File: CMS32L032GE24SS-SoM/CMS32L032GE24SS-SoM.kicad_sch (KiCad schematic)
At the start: 7 parts, among them J105 Connection to DAPLink Board

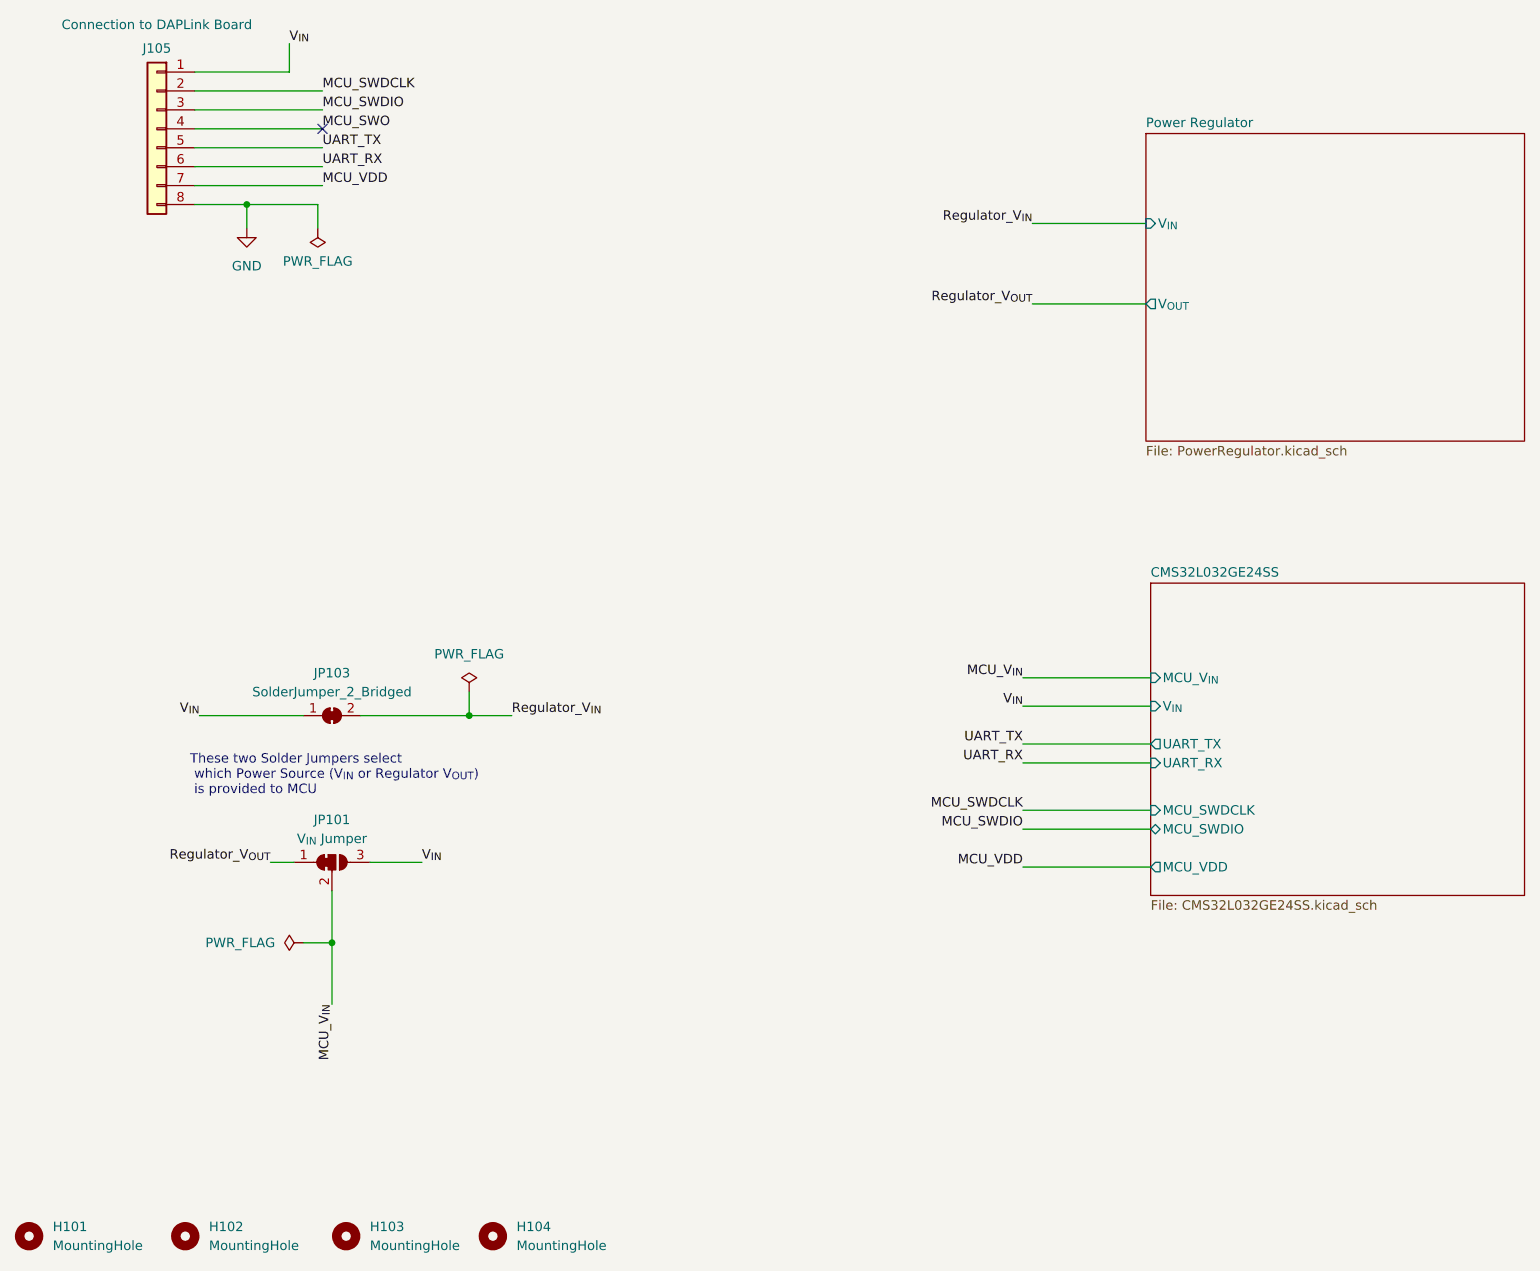
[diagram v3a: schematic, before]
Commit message: changed Power Source jumpers
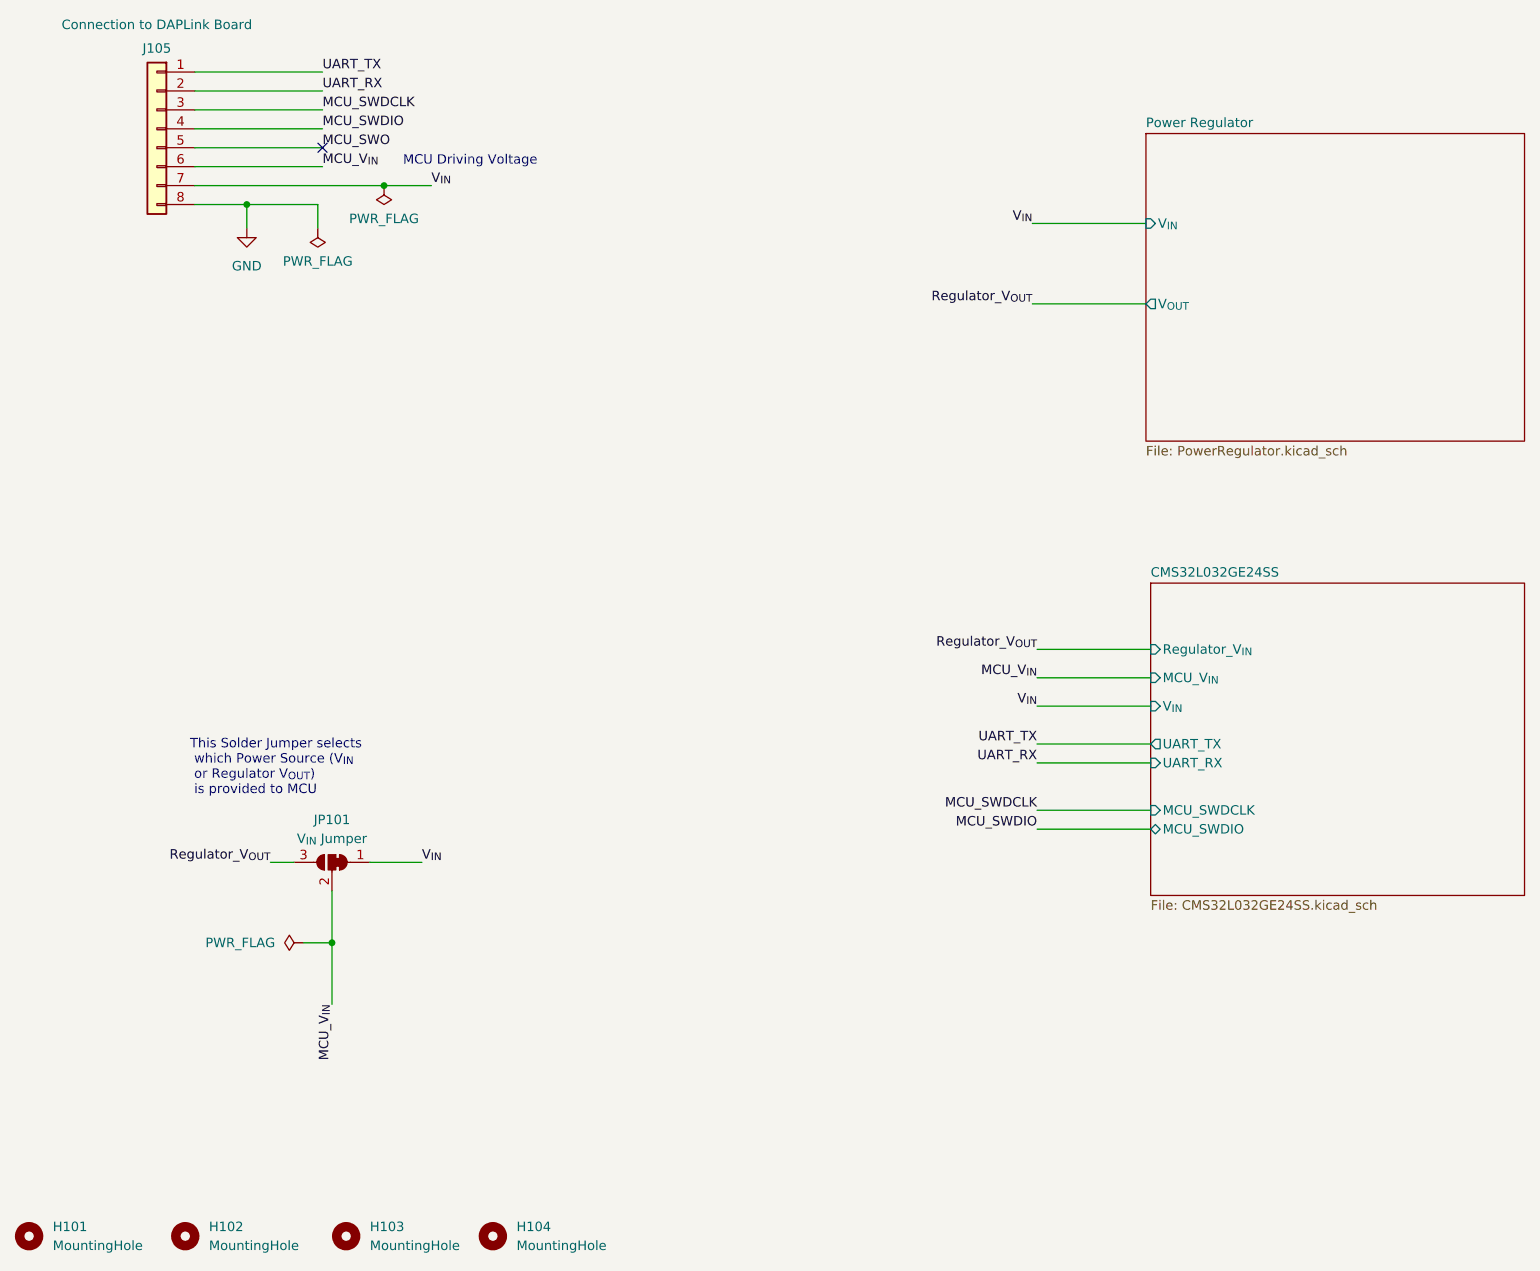
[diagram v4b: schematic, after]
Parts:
- removed JP103: SolderJumper_2_Bridged, Jumper:SolderJumper-2_P1.3mm_Bridged2Bar_RoundedPad1.0x1.5mm, symbol Jumper:SolderJumper_2_Bridged
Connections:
- net MCU_VDD is gone; now on net V_{IN}: J105.7 (Pin_7)
- net MCU_SWDCLK: now also J105.3 (Pin_3); no longer J105.2 (Pin_2)
- net MCU_SWDIO: now also J105.4 (Pin_4); no longer J105.3 (Pin_3)
- net MCU_SWO: now also J105.5 (Pin_5); no longer J105.4 (Pin_4)
- net MCU_V_{IN}: now also J105.6 (Pin_6)
- net Regulator_V_{OUT}: now also JP101.3 (B); no longer JP101.1 (A)
- net UART_RX: now also J105.2 (Pin_2); no longer J105.6 (Pin_6)
- net UART_TX: now also J105.1 (Pin_1); no longer J105.5 (Pin_5)
- net V_{IN}: now also JP101.1 (A); no longer J105.1 (Pin_1), JP101.3 (B)
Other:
- sheet CMS32L032GE24SS ports: added Regulator_V_{IN}; removed MCU_VDD
- note added: "MCU Driving Voltage"
- note added: "This Solder Jumper selects which Power Source (V_{IN} or Regulator V_{OUT}) is provided to MCU"
- note removed: "These two Solder Jumpers select which Power Source (V_{IN} or Regulator V_{OUT}) is provided to MCU"

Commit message: updated Part number in LCSC
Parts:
- J105: LCSC (none) -> C2938418; Vendor (none) -> kinghelm(金航标); Vendor Model (none) -> KH-1.27PH90-1X8P-L10.5
- JP101: now left out of the parts list
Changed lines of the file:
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@@
   )
   (symbol (lib_id "Jumper:SolderJumper_3_Bridged12") (at 65.405 133.35 0) (mirror y) (unit 1)
-    (in_bom yes) (on_board yes) (dnp no)
+    (in_bom no) (on_board yes) (dnp no)
     (property "Reference" "JP101" (at 65.405 127.635 0)
       (effects (font (size 1.27 1.27)))
@@
       (effects (font (size 1.27 1.27)) hide)
     )
-    (property "Description" "" (at 41.91 34.925 0)
+    (property "Description" "排数: 单排 总PIN位数: 8 总PIN位数: 8P 间距: 1.27mm 插针结构: 1x8P 行距: - 安装类型: 弯插 圆针/方针:" (at 41.91 34.925 0)
       (effects (font (size 1.27 1.27)) hide)
     )
-    (property "LCSC" "" (at 41.91 34.925 0)
+    (property "LCSC" "C2938418" (at 41.91 34.925 0)
       (effects (font (size 1.27 1.27)) hide)
     )
-    (property "Vendor" "" (at 41.91 34.925 0)
+    (property "Vendor" "kinghelm(金航标)" (at 41.91 34.925 0)
       (effects (font (size 1.27 1.27)) hide)
     )
-    (property "Vendor Model" "" (at 41.91 34.925 0)
+    (property "Vendor Model" "KH-1.27PH90-1X8P-L10.5" (at 41.91 34.925 0)
       (effects (font (size 1.27 1.27)) hide)
     )
